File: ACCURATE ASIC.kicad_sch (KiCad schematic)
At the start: 74 parts, among them IC11 AD817ARZ, IC12 DAC7578SRGE, IC13 AD817ARZ, IC14 AD817ARZ, IC15 SHT4x, IC16 AD817ARZ, IC17 CERN_aCCURATE2_A_Chip1

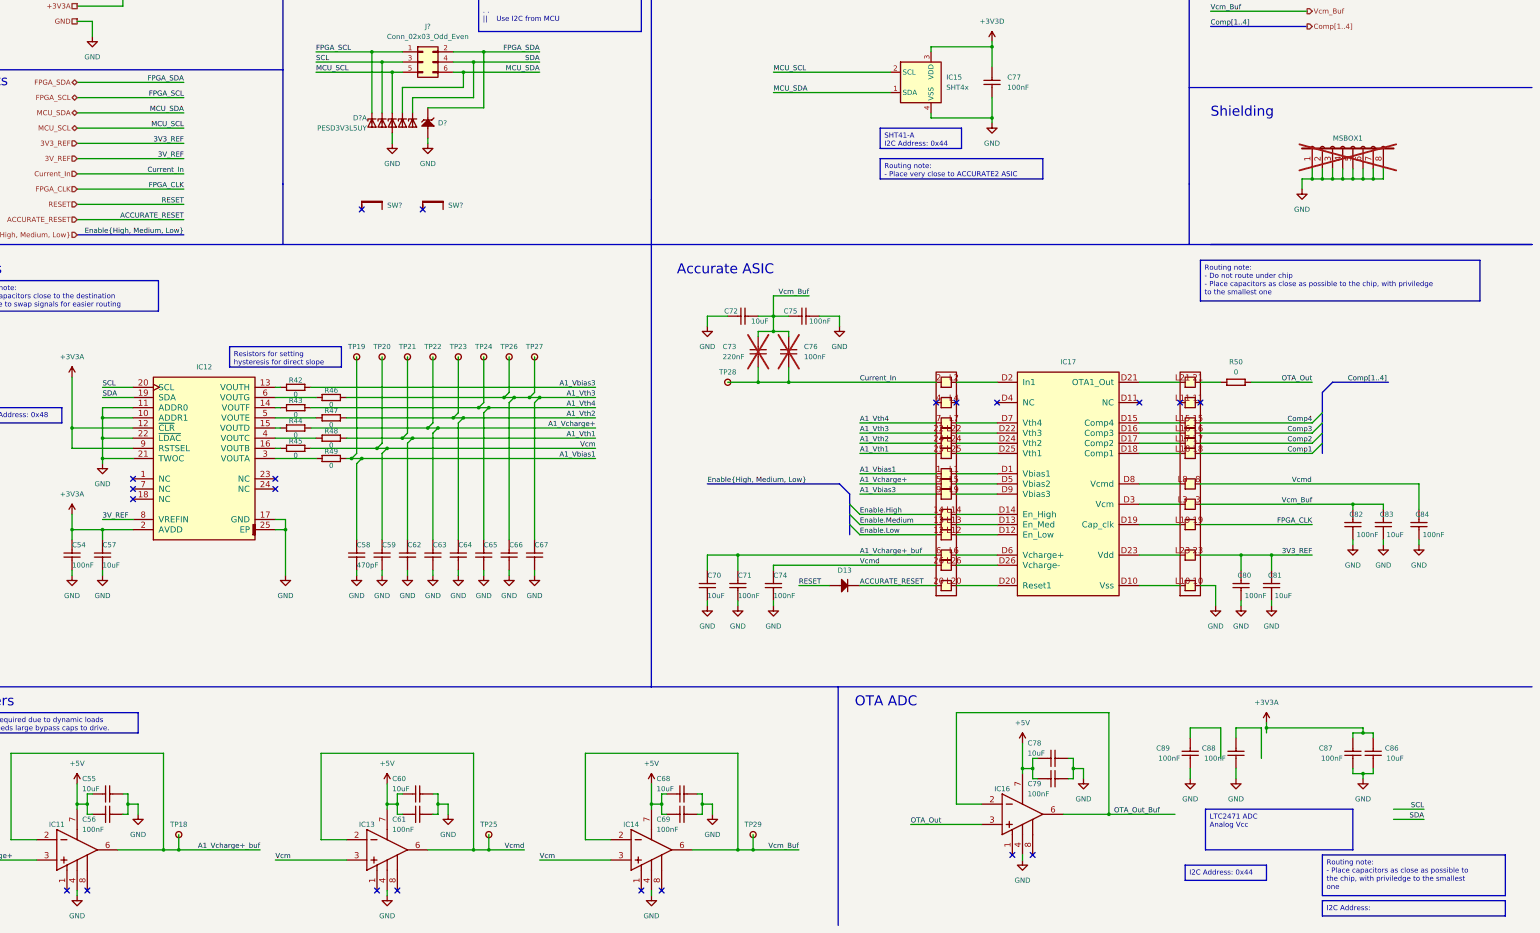
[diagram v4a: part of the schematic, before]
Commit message: Added OTA ADC
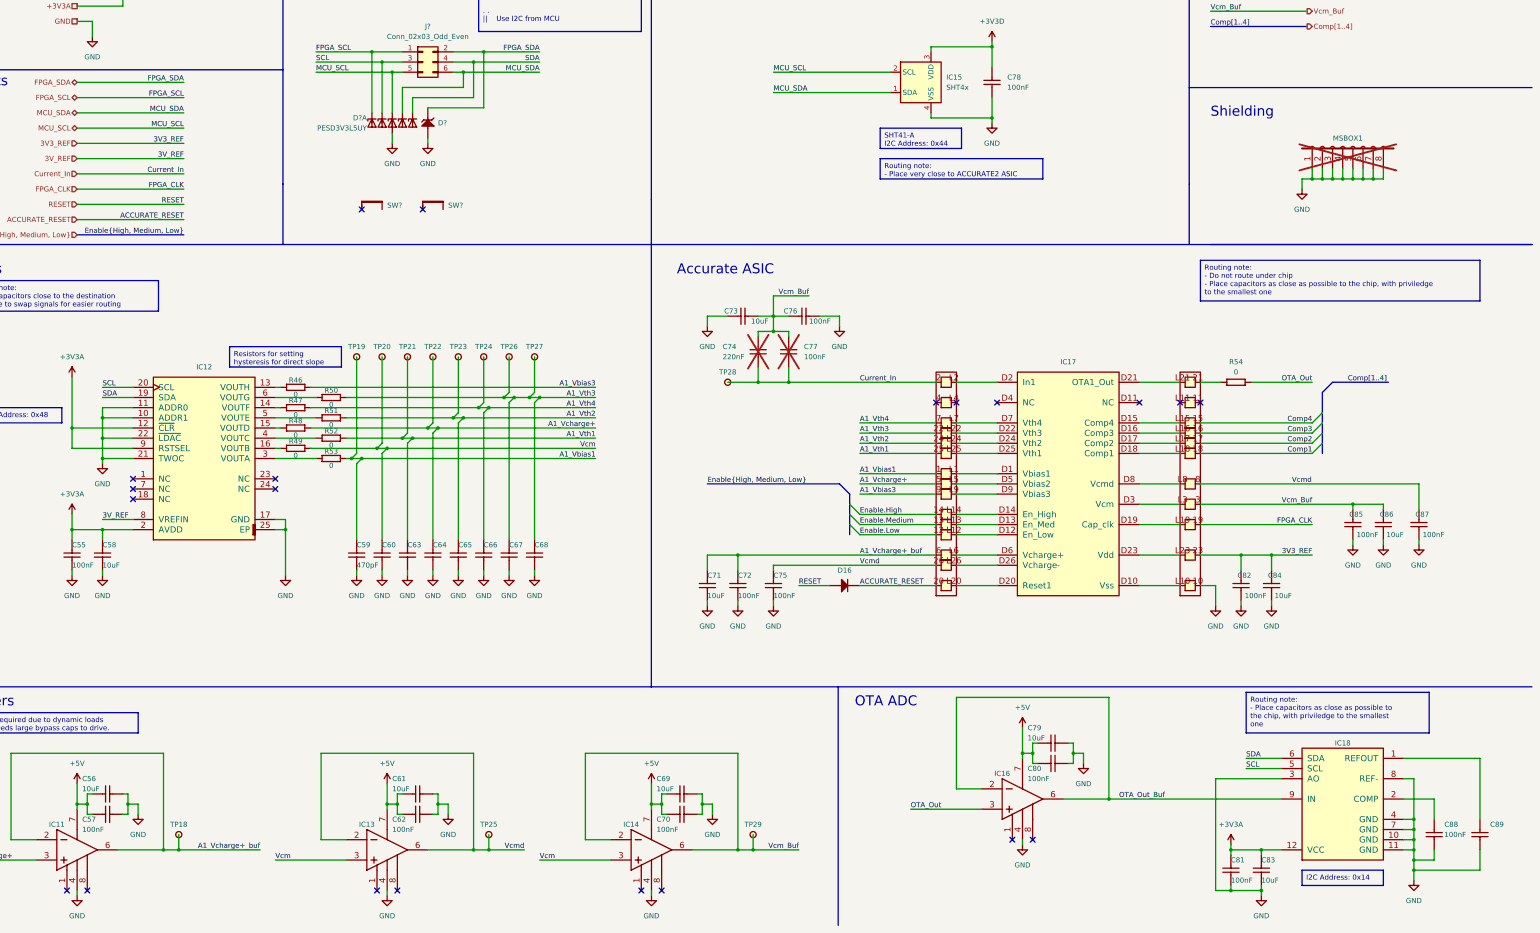
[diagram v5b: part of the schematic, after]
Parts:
- added IC18: LTC2471IMS, ICs And Semiconductors SMD:SOP65P490X110-12N, symbol Analog & Interface:LTC2471IMS
- renumbered C54 to C55, C55 to C56, C56 to C57, C57 to C58, C58 to C59, C59 to C60, C60 to C61, C61 to C62, C62 to C63, C63 to C64, C64 to C65, C65 to C66, C66 to C67, C67 to C68, C68 to C69, C69 to C70, C70 to C71, C71 to C72, C72 to C73, C73 to C74, C74 to C75, C75 to C76, C76 to C77, C77 to C78, C78 to C79, C79 to C80, C87 to C81, C80 to C82, C86 to C83, C81 to C84, C82 to C85, C83 to C86, C84 to C87, D13 to D16, R42 to R46, R43 to R47, R44 to R48, R45 to R49, R46 to R50, R47 to R51, R48 to R52, R49 to R53, R50 to R54
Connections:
- net +3V3A: now also IC18.12 (VCC)
- net GND: now also IC18.10 (GND), IC18.11 (GND), IC18.3 (AO), IC18.4 (GND), IC18.7 (GND), IC18.8 (REF-)
- net OTA_Out_Buf: now also IC18.9 (IN)
- net SCL: now also IC18.5 (SCL)
- net SDA: now also IC18.6 (SDA)
- net at C88.1: now also IC18.2 (COMP)
- net at C89.1: now also IC18.1 (REFOUT)
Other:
- moved on the sheet: C79, C80, C81, C83, C88, C89, IC16

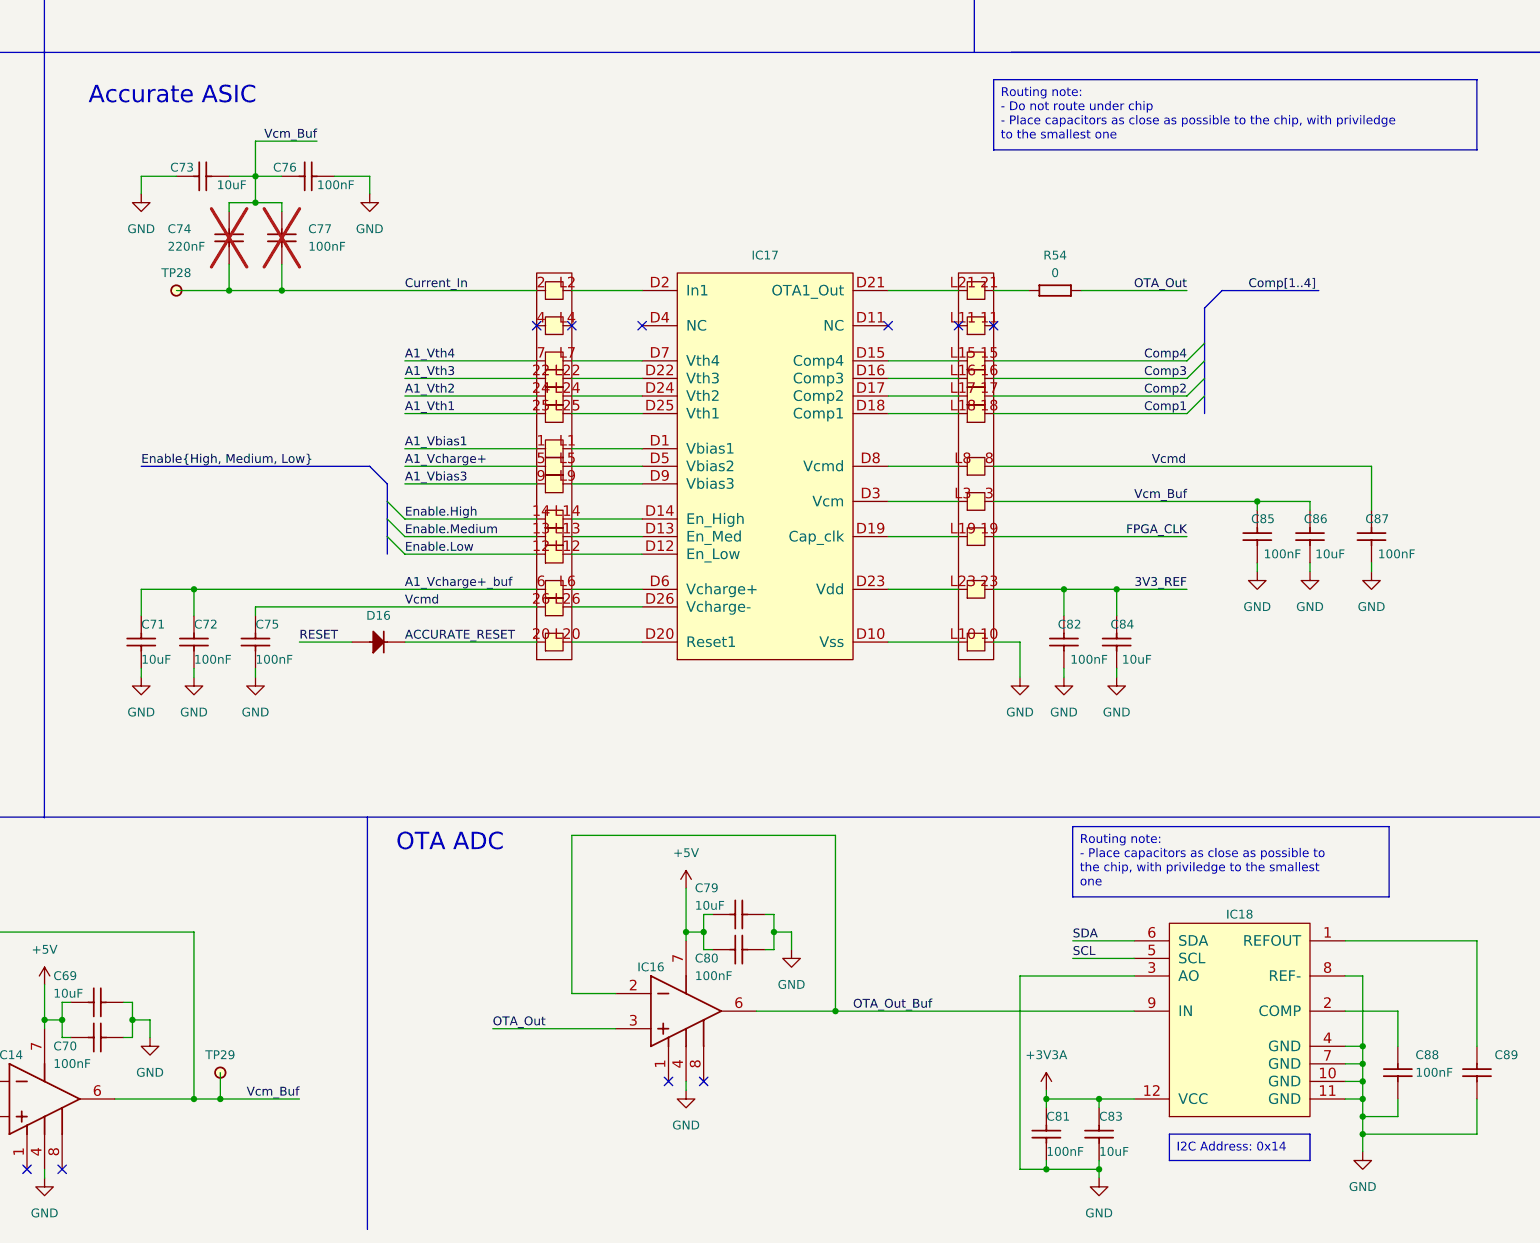
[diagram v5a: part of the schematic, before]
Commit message: Replaced ACCURATE with one that has both packaged and bonded footprint
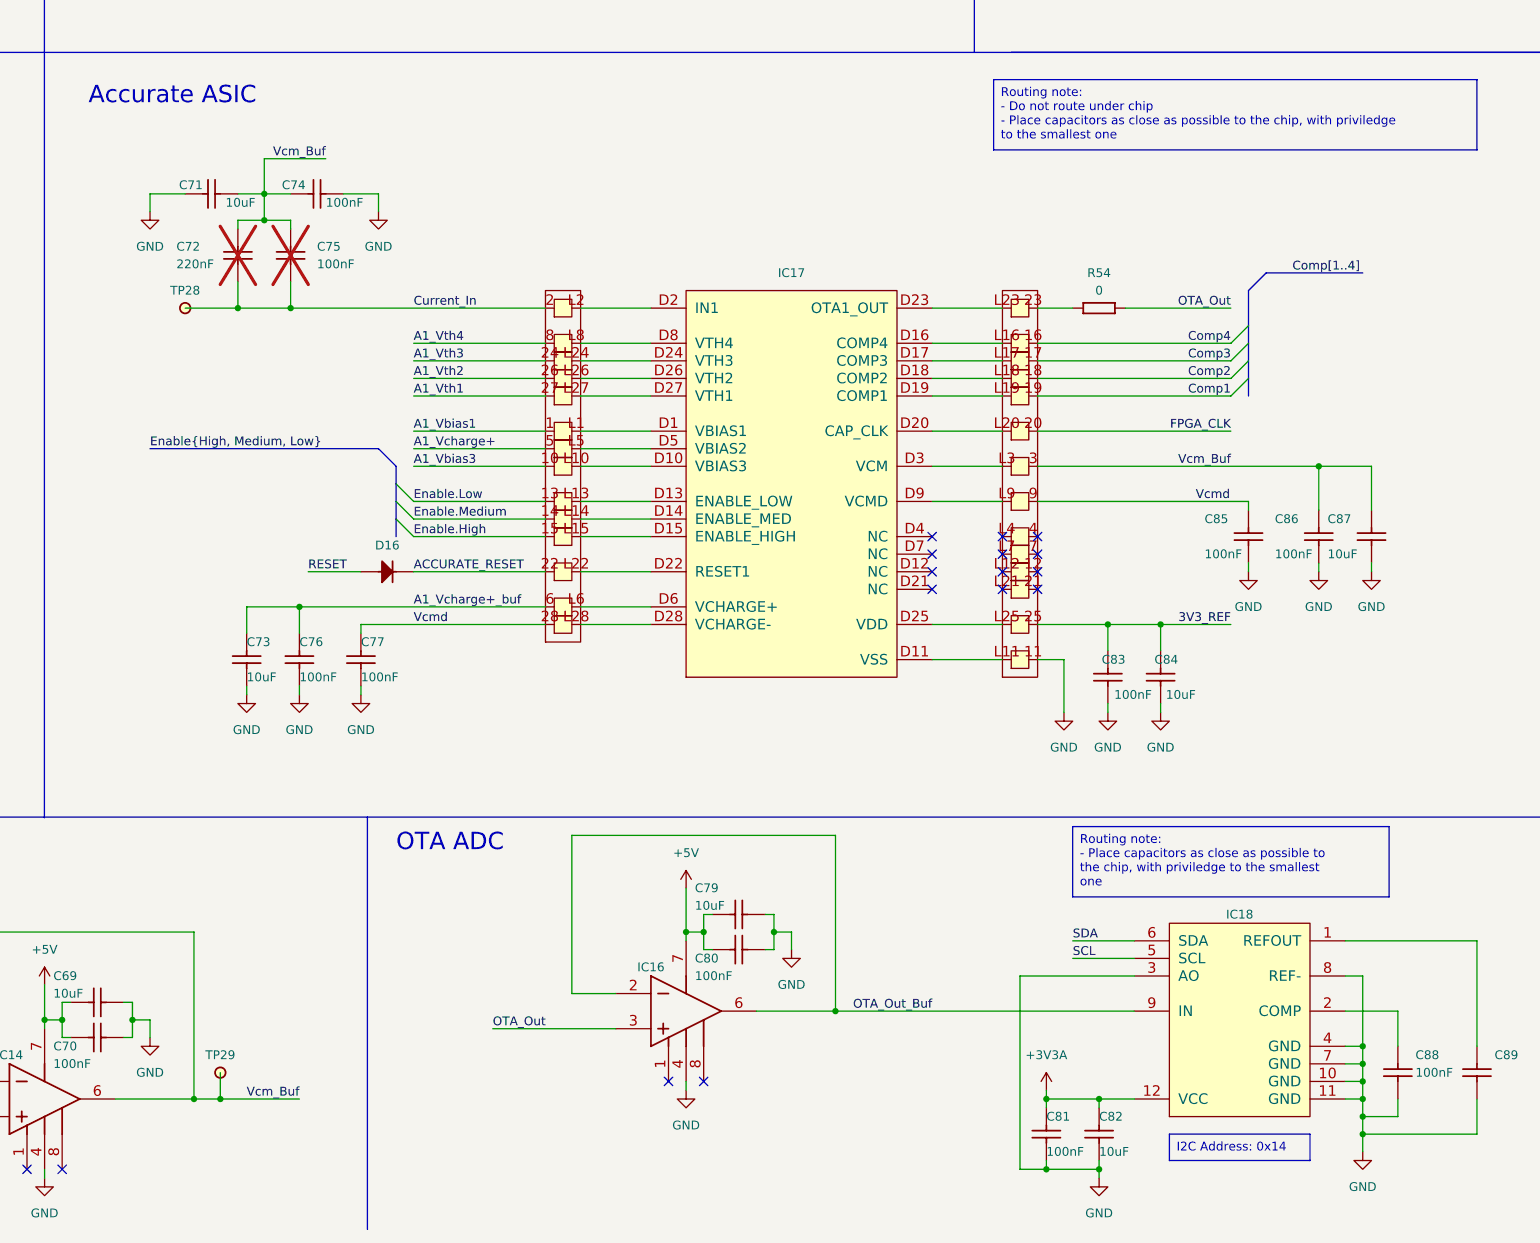
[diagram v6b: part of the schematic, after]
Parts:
- removed C72, C75, C82, C87: CC0603_100NF_50V_10%_X7R, Capacitors SMD:CAPC1608X87N, symbol Capacitors SMD:CC0603_100NF_50V_10%_X7R
- removed C74: CC1206_220NF_16V_10%_X7R, Capacitors SMD:CAPC3216X140N, symbol Capacitors SMD:CC1206_220NF_16V_10%_X7R
- removed C77: CC1206_100NF_50V_10%_X7R, Capacitors SMD:CAPC3216X140N, symbol Capacitors SMD:CC1206_100NF_50V_10%_X7R
- removed C86: CC0603_10UF_25V_20%_X5R, Capacitors SMD:CAPC1709X100N, symbol Capacitors SMD:CC0603_10UF_25V_20%_X5R
- removed IC17: CERN_aCCURATE2_A_Chip1, ICs And Semiconductors Bonding:CERN_aCCURATE1, symbol Bonding:CERN_aCCURATE2_A_Chip1
- added C72: CC1206_220NF_16V_10%_X7R, Capacitors SMD:CAPC3216X140N, symbol Capacitors SMD:CC1206_220NF_16V_10%_X7R
- added C74, C77, C83, C86: CC0603_100NF_50V_10%_X7R, Capacitors SMD:CAPC1608X87N, symbol Capacitors SMD:CC0603_100NF_50V_10%_X7R
- added C75: CC1206_100NF_50V_10%_X7R, Capacitors SMD:CAPC3216X140N, symbol Capacitors SMD:CC1206_100NF_50V_10%_X7R
- added C87: CC0603_10UF_25V_20%_X5R, Capacitors SMD:CAPC1709X100N, symbol Capacitors SMD:CC0603_10UF_25V_20%_X5R
- added IC17: CERN_ACCURATE_2A, ICs And Semiconductors Bonding:CERN_ACCURATE_2A, symbol Bonding:CERN_ACCURATE_2A
- renumbered C83 to C82
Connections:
- net 3V3_REF: now also C83.1, IC17.25
- net A1_Vbias1: now also IC17.1
- net A1_Vbias3: now also IC17.10
- net A1_Vcharge+: now also IC17.5
- net A1_Vcharge+_buf: now also C73.1, C76.1, IC17.6; no longer C71.1
- net A1_Vth1: now also IC17.27
- net A1_Vth2: now also IC17.26
- net A1_Vth3: now also IC17.24
- net A1_Vth4: now also IC17.8
- net ACCURATE_RESET: now also IC17.22
- net Comp1: now also IC17.19
- net Comp2: now also IC17.18
- net Comp3: now also IC17.17
- net Comp4: now also IC17.16
- net Current_In: now also C72.2, C75.2, IC17.2
- net Enable.High: now also IC17.15
- net Enable.Low: now also IC17.13
- net Enable.Medium: now also IC17.14
- net FPGA_CLK: now also IC17.20
- net GND: now also C74.2, C77.2, C83.2, C86.2, C87.2, IC17.11
- net Vcm_Buf: now also C71.1, C72.1, C74.1, C75.1, C86.1, C87.1, IC17.3; no longer C73.1, C76.1, C85.1
- net Vcmd: now also C85.1, C77.1, IC17.28, IC17.9
- net at R54.1: now also IC17.23
- new net: IC17.D1 (VBIAS1), IC17.L1
- new net: IC17.D10 (VBIAS3), IC17.L10
- new net: IC17.D11 (VSS), IC17.L11
- new net: IC17.D13 (ENABLE_LOW), IC17.L13
- new net: IC17.D14 (ENABLE_MED), IC17.L14
- new net: IC17.D15 (ENABLE_HIGH), IC17.L15
- new net: IC17.D16 (COMP4), IC17.L16
- new net: IC17.D17 (COMP3), IC17.L17
- new net: IC17.D18 (COMP2), IC17.L18
- new net: IC17.D19 (COMP1), IC17.L19
- new net: IC17.D2 (IN1), IC17.L2
- new net: IC17.D20 (CAP_CLK), IC17.L20
- new net: IC17.D22 (RESET1), IC17.L22
- new net: IC17.D23 (OTA1_OUT), IC17.L23
- new net: IC17.D24 (VTH3), IC17.L24
- new net: IC17.D25 (VDD), IC17.L25
- new net: IC17.D26 (VTH2), IC17.L26
- new net: IC17.D27 (VTH1), IC17.L27
- new net: IC17.D28 (VCHARGE-), IC17.L28
- new net: IC17.D3 (VCM), IC17.L3
- new net: IC17.D5 (VBIAS2), IC17.L5
- new net: IC17.D6 (VCHARGE+), IC17.L6
- new net: IC17.D8 (VTH4), IC17.L8
- new net: IC17.D9 (VCMD), IC17.L9
- no-connect marks 21 -> 27

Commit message: Switched to iCE5LP4K, added power switch and 3V ref
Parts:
- renumbered IC11 to IC12, IC12 to IC13, IC13 to IC14, IC14 to IC15, IC15 to IC16, IC16 to IC17, IC17 to IC18, IC18 to IC19

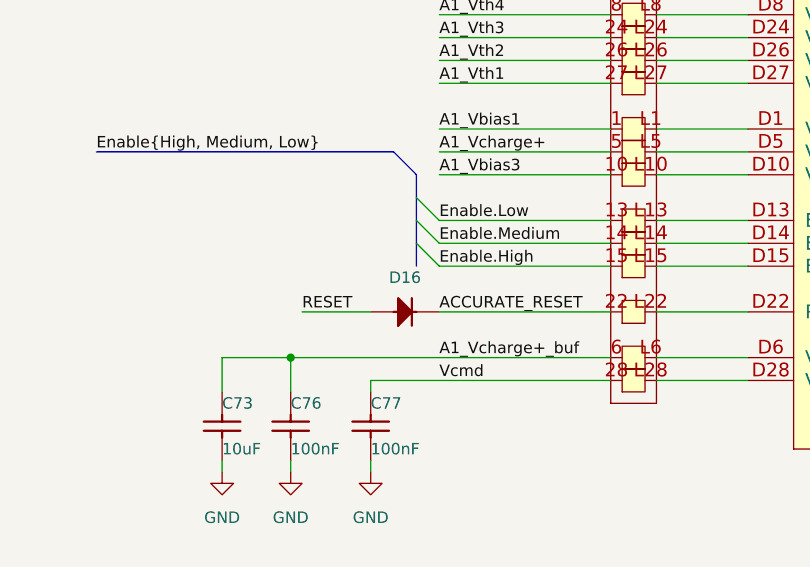
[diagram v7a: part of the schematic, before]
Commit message: Fixed DRC errors and warnings
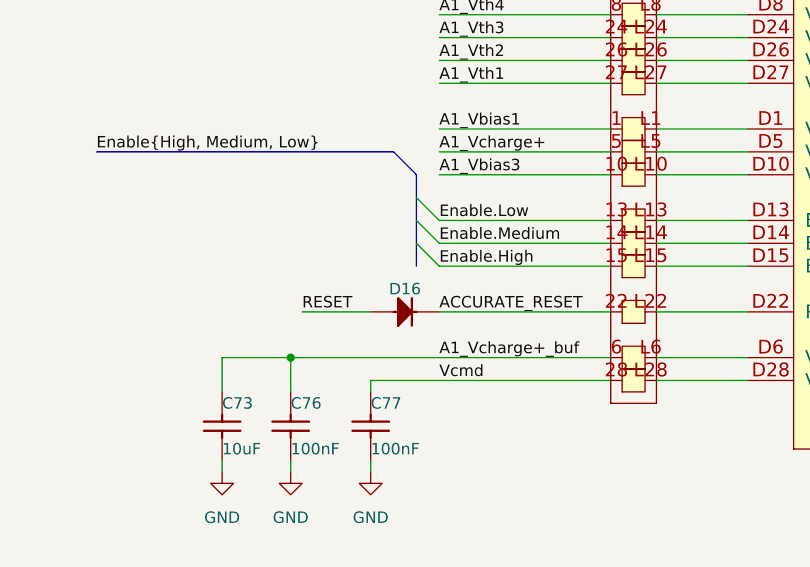
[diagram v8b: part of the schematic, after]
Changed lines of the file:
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@@
   )
   (symbol (lib_id "Diodes:1N4148WS") (at 233.68 165.1 0) (unit 1)
-    (in_bom yes) (on_board yes) (dnp no) (fields_autoplaced)
-    (property "Reference" "D16" (at 237.49 161.29 0)
+    (in_bom yes) (on_board yes) (dnp no)
+    (property "Reference" "D16" (at 237.49 162.56 0)
       (effects (font (size 1.27 1.27)))
     )
